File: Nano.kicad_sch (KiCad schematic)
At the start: 32 parts, among them J3 Flash, J4 ICSP, J5 LCD, J6 RJ45, SW1 Page, U5 ATmega644P-20A, U6 MCP2515-xST, U7 TJA1050T, Y1 12MHz, Y2 12MHz

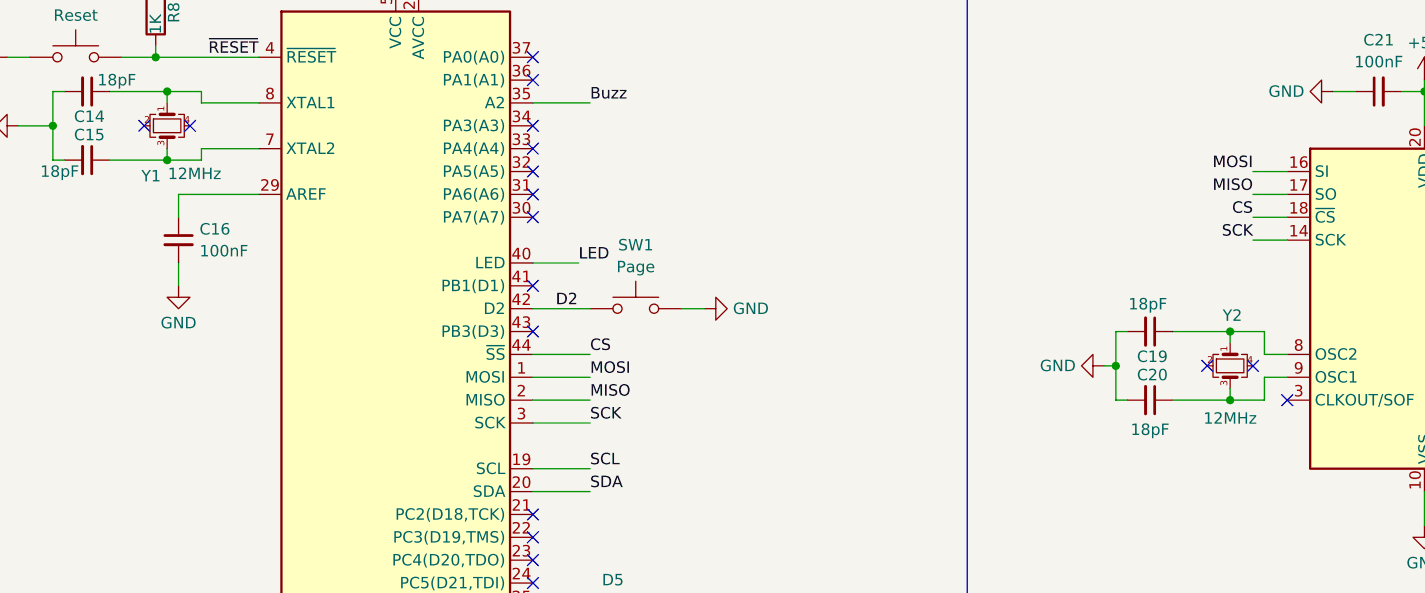
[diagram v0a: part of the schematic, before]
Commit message: changed the crystal to 16MHz
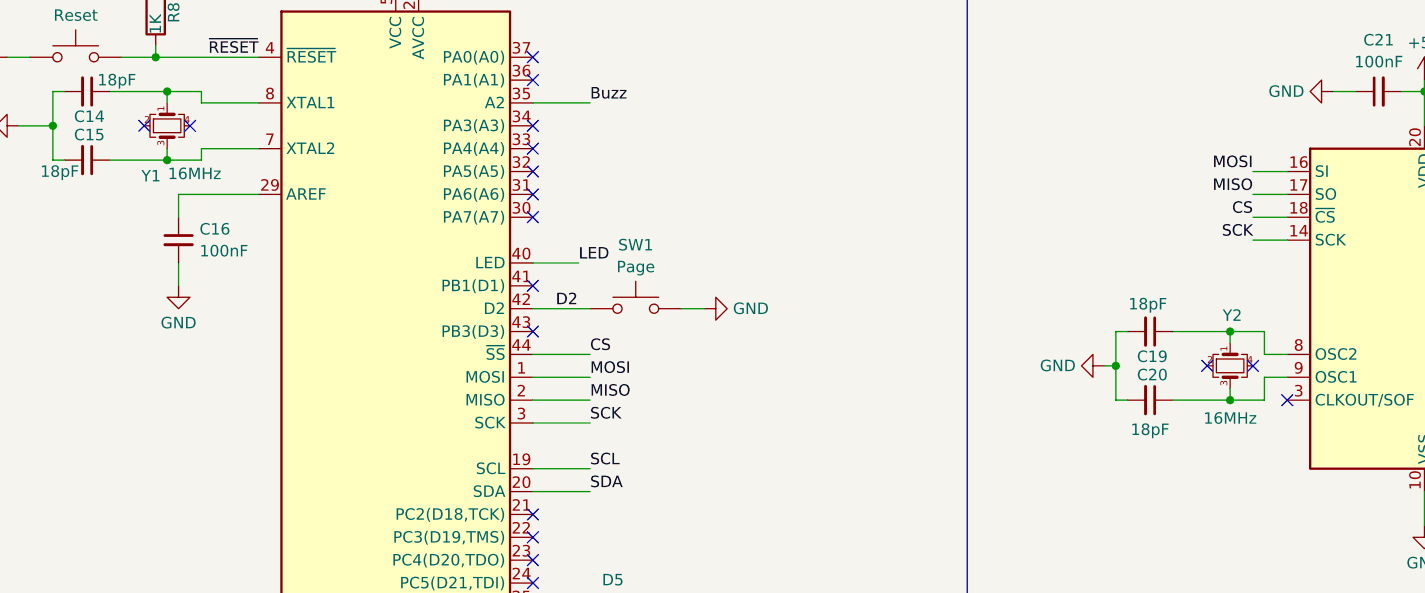
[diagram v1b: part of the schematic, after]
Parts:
- Y1, Y2: value 12MHz -> 16MHz
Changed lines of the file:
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@@
 			)
 		)
-		(property "Value" "12MHz"
+		(property "Value" "16MHz"
 			(at 50.038 101.854 90)
 			(effects
@@
 			)
 		)
-		(property "Value" "12MHz"
+		(property "Value" "16MHz"
 			(at 165.1 129.032 90)
 			(effects

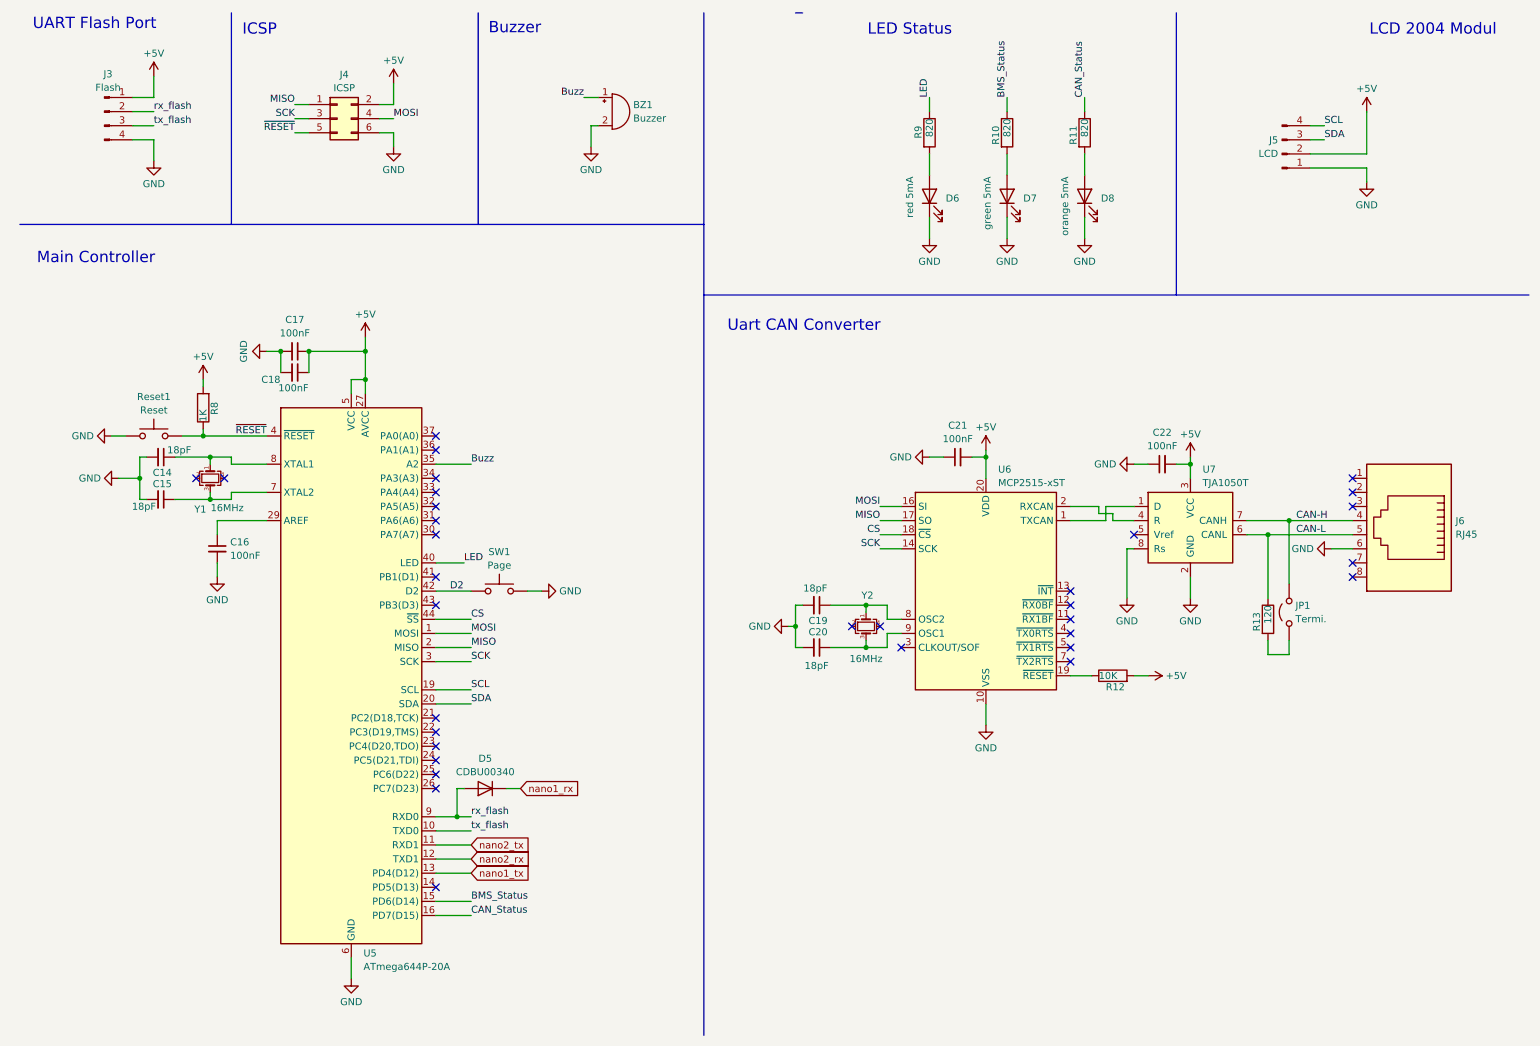
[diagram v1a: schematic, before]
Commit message: changed to rev 1.1
added DTR line for easy flashing
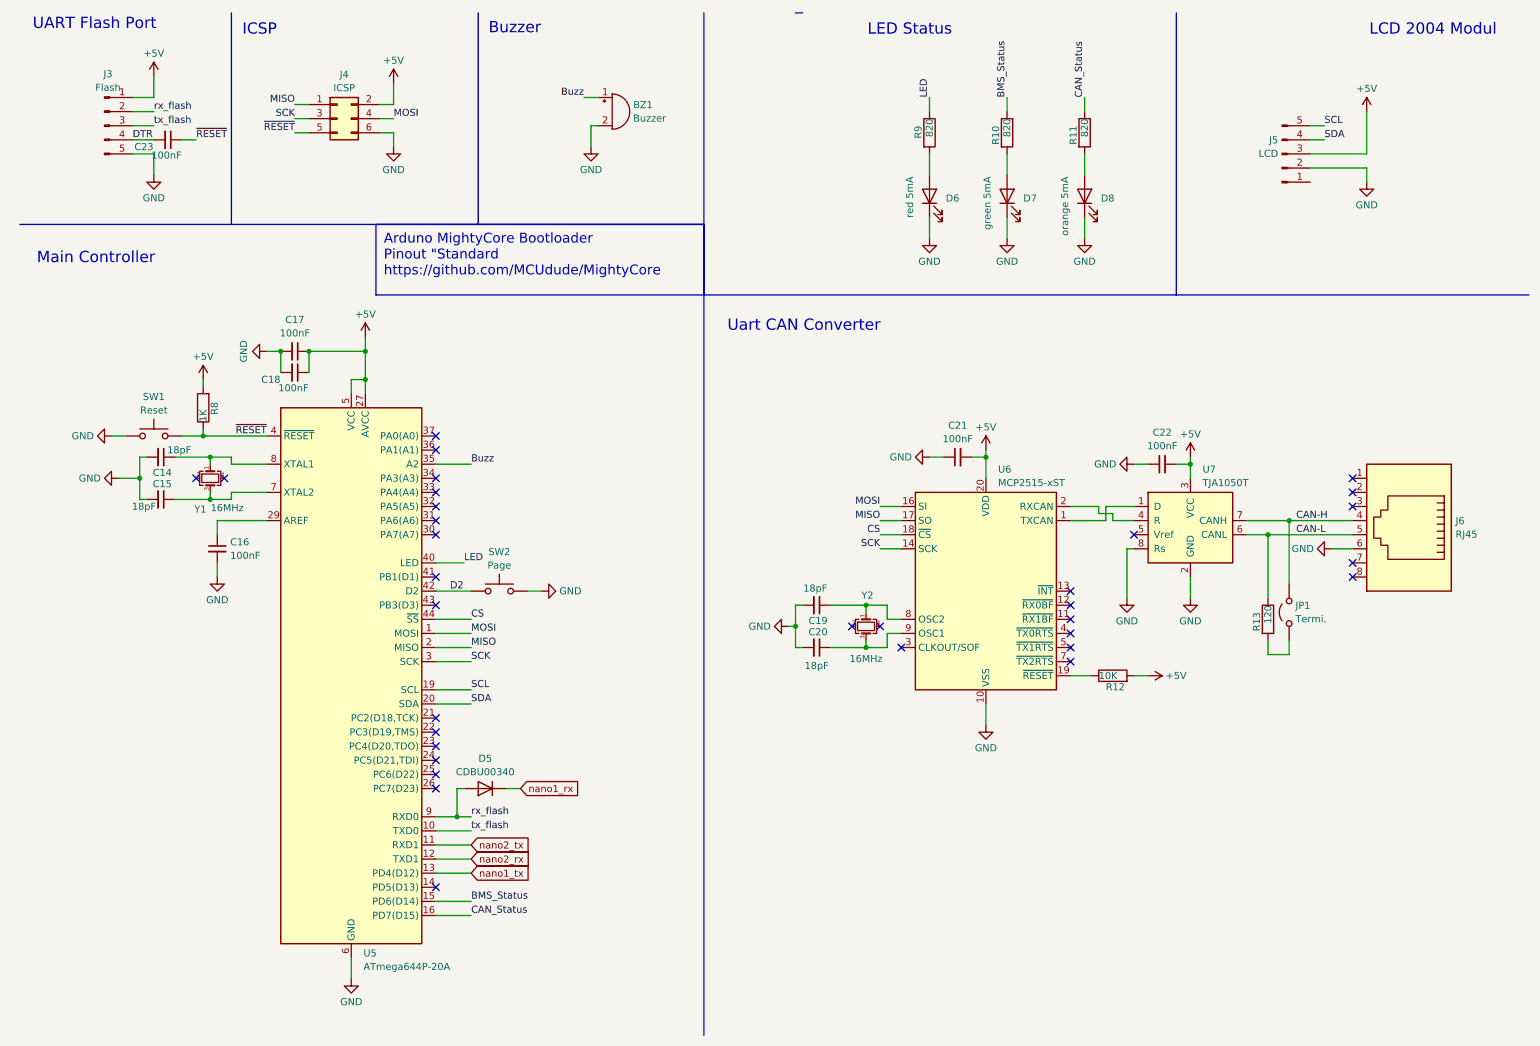
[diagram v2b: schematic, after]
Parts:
- added C23: 100nF, Capacitor_SMD:C_0603_1608Metric_Pad1.08x0.95mm_HandSolder, symbol Device:C_Small
- J3: footprint Connector_PinHeader_2.54mm:PinHeader_1x04_P2.54mm_Vertical -> Connector_PinHeader_2.54mm:PinHeader_1x05_P2.54mm_Vertical; symbol Connector:Conn_01x04_Pin -> Connector:Conn_01x05_Pin
- J5: symbol Connector:Conn_01x04_Pin -> Connector:Conn_01x05_Pin
- renumbered Reset1 to SW1, SW1 to SW2
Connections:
- net +5V: now also J5.3 (Pin_3); no longer J5.2 (Pin_2)
- net GND: now also J3.5 (Pin_5), J5.2 (Pin_2); no longer J3.4 (Pin_4), J5.1 (Pin_1)
- net SCL: now also J5.5 (Pin_5); no longer J5.4 (Pin_4)
- net SDA: now also J5.4 (Pin_4); no longer J5.3 (Pin_3)
- net ~{RESET}: now also C23.1
- new net DTR: C23.2, J3.4 (Pin_4)
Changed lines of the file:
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@@
 	(wire
 		(pts
+			(xy 33.02 35.56) (xy 36.83 35.56)
+		)
+		(stroke
+			(width 0)
+			(type default)
+		)
+	)
+	(wire
+		(pts
 			(xy 186.69 91.44) (xy 186.69 92.71)
 		)
@@
 	(wire
 		(pts
-			(xy 33.02 35.56) (xy 36.83 35.56)
+			(xy 33.02 38.1) (xy 36.83 38.1)
 		)
 		(stroke
@@
 	(wire
 		(pts
-			(xy 36.83 35.56) (xy 36.83 39.37)
+			(xy 36.83 38.1) (xy 36.83 41.91)
 		)
 		(stroke
@@
 	(wire
 		(pts
+			(xy 41.91 35.56) (xy 44.45 35.56)
+		)
+		(stroke
+			(width 0)
+			(type default)
+		)
+	)
+	(wire
+		(pts
 			(xy 33.02 27.94) (xy 36.83 27.94)
 		)
@@
 		)
 	)
+	(text_box "Arduno MightyCore Bootloader\nPinout \"Standard\nhttps://github.com/MCUdude/MightyCore"
+		(exclude_from_sim no)
+		(at 76.835 50.8 0)
+		(size 59.055 12.7)
+		(stroke
+			(width 0)
+			(type default)
+		)
+		(fill
+			(type none)
+		)
+		(effects
+			(font
+				(size 1.778 1.778)
+			)
+			(justify left top)
+		)
+	)
 	(text "LCD 2004 Modul"
 		(exclude_from_sim no)
@@
 		)
 	)
+	(label "DTR"
+		(at 33.02 35.56 0)
+		(fields_autoplaced yes)
+		(effects
+			(font
+				(size 1.27 1.27)
+			)
+			(justify left bottom)
+		)
+	)
 	(label "SCK"
 		(at 62.23 31.75 180)
@@
 		)
 	)
+	(label "~{RESET}"
+		(at 44.45 35.56 0)
+		(fields_autoplaced yes)
+		(effects
+			(font
+				(size 1.27 1.27)
+			)
+			(justify left bottom)
+		)
+	)
 	(label "D2"
 		(at 90.17 116.84 0)
@@
 		(dnp no)
 		(fields_autoplaced yes)
-		(property "Reference" "SW1"
+		(property "Reference" "SW2"
 			(at 99.06 109.7747 0)
 			(effects
@@
 			(project "JK-BMS_CAN"
 				(path "/d82ff742-6f7f-4a3b-883a-5922801ae813/49db526c-fdfa-49f8-940f-9cb274099387"
-					(reference "SW1")
+					(reference "SW2")
 					(unit 1)
 				)
@@
 	)
 	(symbol
-		(lib_id "Connector:Conn_01x04_Pin")
+		(lib_id "Connector:Conn_01x05_Pin")
 		(at 240.03 38.1 0)
 		(mirror x)
@@
 			)
 		)
-		(property "Description" "Generic connector, single row, 01x04, script generated"
+		(property "Description" "Generic connector, single row, 01x05, script generated"
 			(at 240.03 38.1 0)
 			(effects
@@
 		(pin "4"
 		)
+		(pin "5"
+		)
 		(instances
 			(project "JK-BMS_CAN"
@@
 	(symbol
 		(lib_id "power:GND")
-		(at 36.83 39.37 0)
+		(at 36.83 41.91 0)
 		(unit 1)
 		(exclude_from_sim no)
@@
 		(fields_autoplaced yes)
 		(property "Reference" "#PWR032"
-			(at 36.83 45.72 0)
+			(at 36.83 48.26 0)
 			(effects
 				(font
@@
 		)
 		(property "Value" "GND"
-			(at 36.83 43.5031 0)
+			(at 36.83 46.0431 0)
 			(effects
 				(font
@@
 		)
 		(property "Footprint" ""
-			(at 36.83 39.37 0)
+			(at 36.83 41.91 0)
 			(effects
 				(font
@@
 		)
 		(property "Datasheet" ""
-			(at 36.83 39.37 0)
+			(at 36.83 41.91 0)
 			(effects
 				(font
@@
 		)
 		(property "Description" "Power symbol creates a global label with name \"GND\" , ground"
-			(at 36.83 39.37 0)
+			(at 36.83 41.91 0)
 			(effects
 				(font
@@
 	)
 	(symbol
+		(lib_id "Device:C_Small")
+		(at 39.37 35.56 270)
+		(unit 1)
+		(exclude_from_sim no)
+		(in_bom yes)
+		(on_board yes)
+		(dnp no)
+		(property "Reference" "C23"
+			(at 35.052 36.83 90)
+			(effects
+				(font
+					(size 1.27 1.27)
+				)
+			)
+		)
+		(property "Value" "100nF"
+			(at 39.116 38.354 90)
+			(effects
+				(font
+					(size 1.27 1.27)
+				)
+			)
+		)
+		(property "Footprint" "Capacitor_SMD:C_0603_1608Metric_Pad1.08x0.95mm_HandSolder"
+			(at 39.37 35.56 0)
+			(effects
+				(font
+					(size 1.27 1.27)
+				)
+				(hide yes)
+			)
+		)
+		(property "Datasheet" "~"
+			(at 39.37 35.56 0)
+			(effects
+				(font
+					(size 1.27 1.27)
+				)
+				(hide yes)
+			)
+		)
+		(property "Description" "Unpolarized capacitor, small symbol"
+			(at 39.37 35.56 0)
+			(effects
+				(font
+					(size 1.27 1.27)
+				)
+				(hide yes)
+			)
+		)
+		(property "Part Number" ""
+			(at 39.37 35.56 0)
+			(effects
+				(font
+					(size 1.27 1.27)
+				)
+				(hide yes)
+			)
+		)
+		(pin "2"
+		)
+		(pin "1"
+		)
+		(instances
+			(project "JK-BMS_CAN"
+				(path "/d82ff742-6f7f-4a3b-883a-5922801ae813/49db526c-fdfa-49f8-940f-9cb274099387"
+					(reference "C23")
+					(unit 1)
+				)
+			)
+		)
+	)
+	(symbol
 		(lib_id "ATmega164-324-644-128:ATmega644P-20A")
 		(at 72.39 132.08 0)
@@
 	)
 	(symbol
-		(lib_id "Connector:Conn_01x04_Pin")
-		(at 27.94 30.48 0)
+		(lib_id "Connector:Conn_01x05_Pin")
+		(at 27.94 33.02 0)
 		(unit 1)
 		(exclude_from_sim no)
@@
 			)
 		)
-		(property "Footprint" "Connector_PinHeader_2.54mm:PinHeader_1x04_P2.54mm_Vertical"
-			(at 27.94 30.48 0)
+		(property "Footprint" "Connector_PinHeader_2.54mm:PinHeader_1x05_P2.54mm_Vertical"
+			(at 27.94 33.02 0)
 			(effects
 				(font
@@
 		)
 		(property "Datasheet" "~"
-			(at 27.94 30.48 0)
+			(at 27.94 33.02 0)
 			(effects
 				(font
@@
 			)
 		)
-		(property "Description" "Generic connector, single row, 01x04, script generated"
-			(at 27.94 30.48 0)
+		(property "Description" "Generic connector, single row, 01x05, script generated"
+			(at 27.94 33.02 0)
 			(effects
 				(font
@@
 		(pin "1"
 		)
+		(pin "5"
+		)
 		(instances
 			(project "JK-BMS_CAN"
@@
 		(dnp no)
 		(fields_autoplaced yes)
-		(property "Reference" "Reset1"
+		(property "Reference" "SW1"
 			(at 36.83 81.8345 0)
 			(effects
@@
 			(project "JK-BMS_CAN"
 				(path "/d82ff742-6f7f-4a3b-883a-5922801ae813/49db526c-fdfa-49f8-940f-9cb274099387"
-					(reference "Reset1")
+					(reference "SW1")
 					(unit 1)
 				)
